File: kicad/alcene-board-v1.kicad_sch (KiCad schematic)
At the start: 3 parts, among them J1 ESP32-S3-DevKitC-1_J1, J3 ESP32-S3-DevKitC-1_J3, J4 ILI9341_TFT_14pin

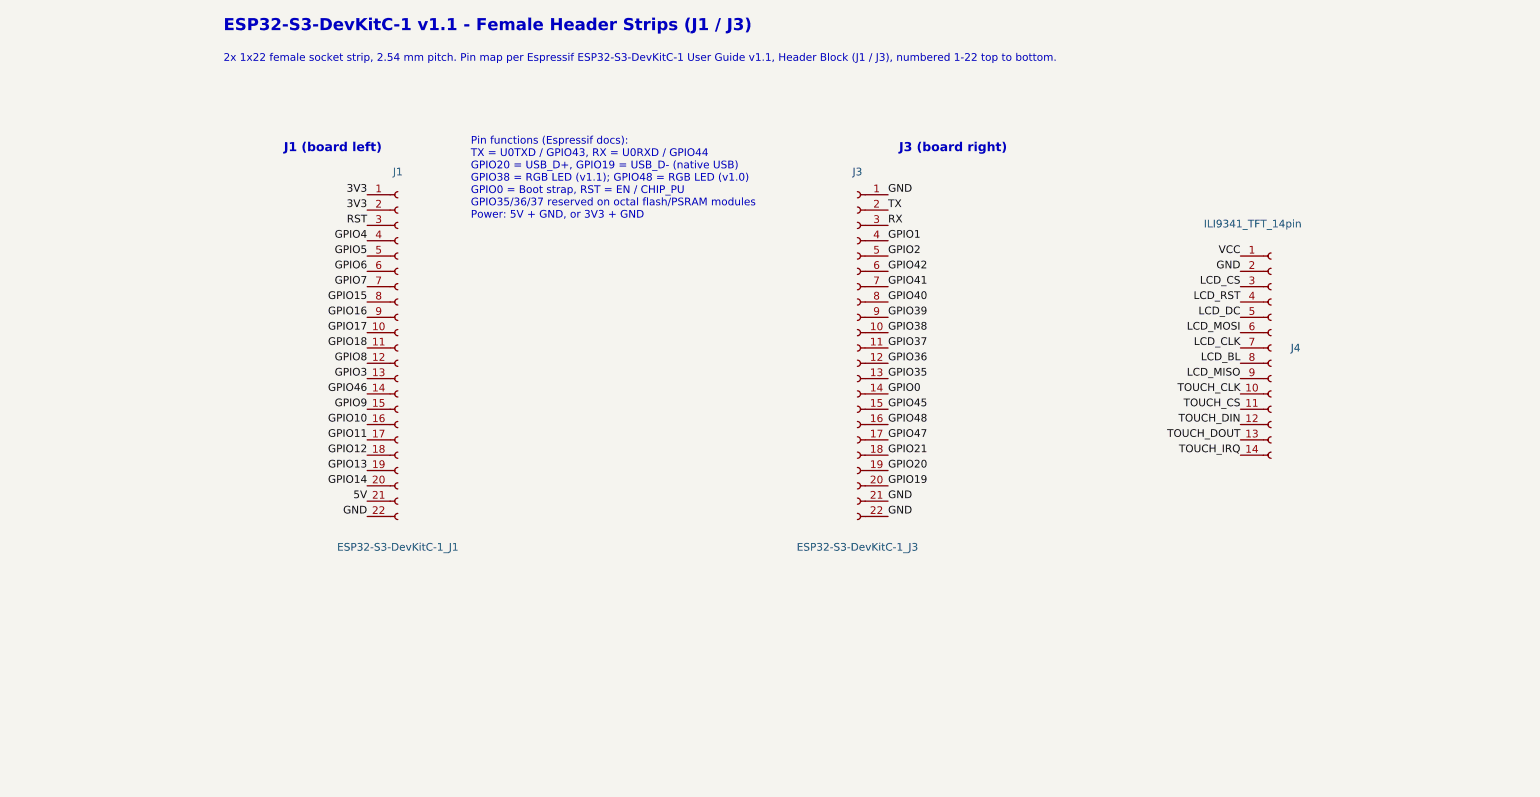
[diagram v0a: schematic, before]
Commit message: feat: wiring ILI9341 pin labels to ESP32 S3
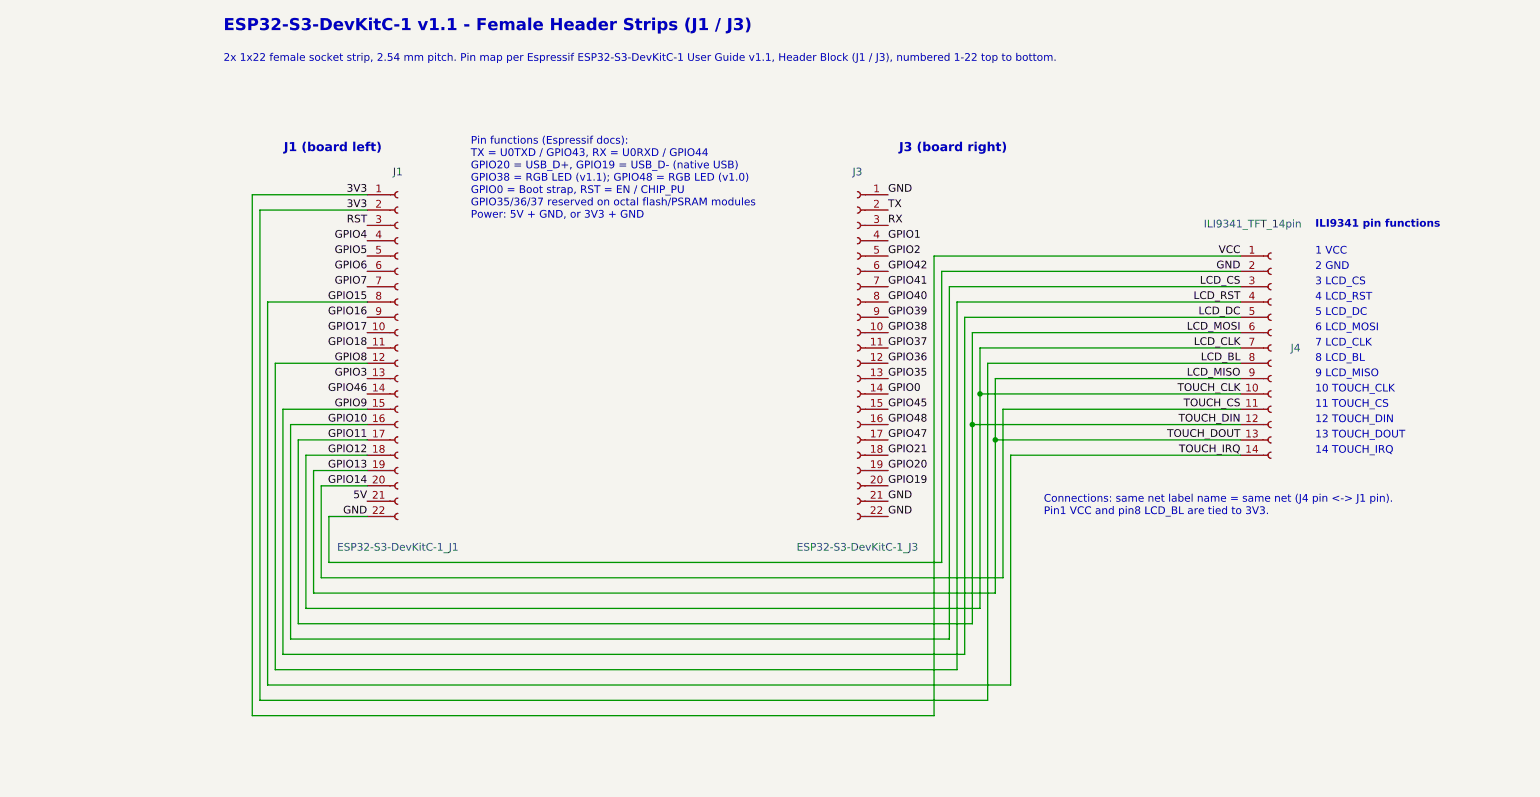
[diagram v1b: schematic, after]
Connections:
- net LCD_BL is gone; now on net 3V3: J4.8 (Pin_8)
- net LCD_CLK is gone; now on net GPIO12: J4.7 (Pin_7)
- net LCD_CS is gone; now on net GPIO10: J4.3 (Pin_3)
- net LCD_DC is gone; now on net GPIO9: J4.5 (Pin_5)
- net LCD_MISO is gone; now on net GPIO13: J4.9 (Pin_9)
- net LCD_MOSI is gone; now on net GPIO11: J4.6 (Pin_6)
- net LCD_RST is gone; now on net GPIO8: J4.4 (Pin_4)
- net TOUCH_CLK is gone; now on net GPIO12: J4.10 (Pin_10)
- net TOUCH_CS is gone; now on net GPIO14: J4.11 (Pin_11)
- net TOUCH_DIN is gone; now on net GPIO11: J4.12 (Pin_12)
- net TOUCH_DOUT is gone; now on net GPIO13: J4.13 (Pin_13)
- net TOUCH_IRQ is gone; now on net GPIO15: J4.14 (Pin_14)
- net VCC is gone; now on net 3V3: J4.1 (Pin_1)
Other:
- note added: "1 VCC"
- note added: "10 TOUCH_CLK"
- note added: "11 TOUCH_CS"
- note added: "12 TOUCH_DIN"
- note added: "13 TOUCH_DOUT"
- note added: "14 TOUCH_IRQ"
- note added: "2 GND"
- note added: "3 LCD_CS"
- note added: "4 LCD_RST"
- note added: "5 LCD_DC"
- note added: "6 LCD_MOSI"
- note added: "7 LCD_CLK"
- note added: "8 LCD_BL"
- note added: "9 LCD_MISO"
- note added: "Connections: same net label name = same net (J4 pin <-> J1 pin). Pin1 VCC and pin8 LCD_BL are tied to 3V3."
- note added: "ILI9341 pin functions"

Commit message: feat: wiring TFT and ESP32 headers and labels
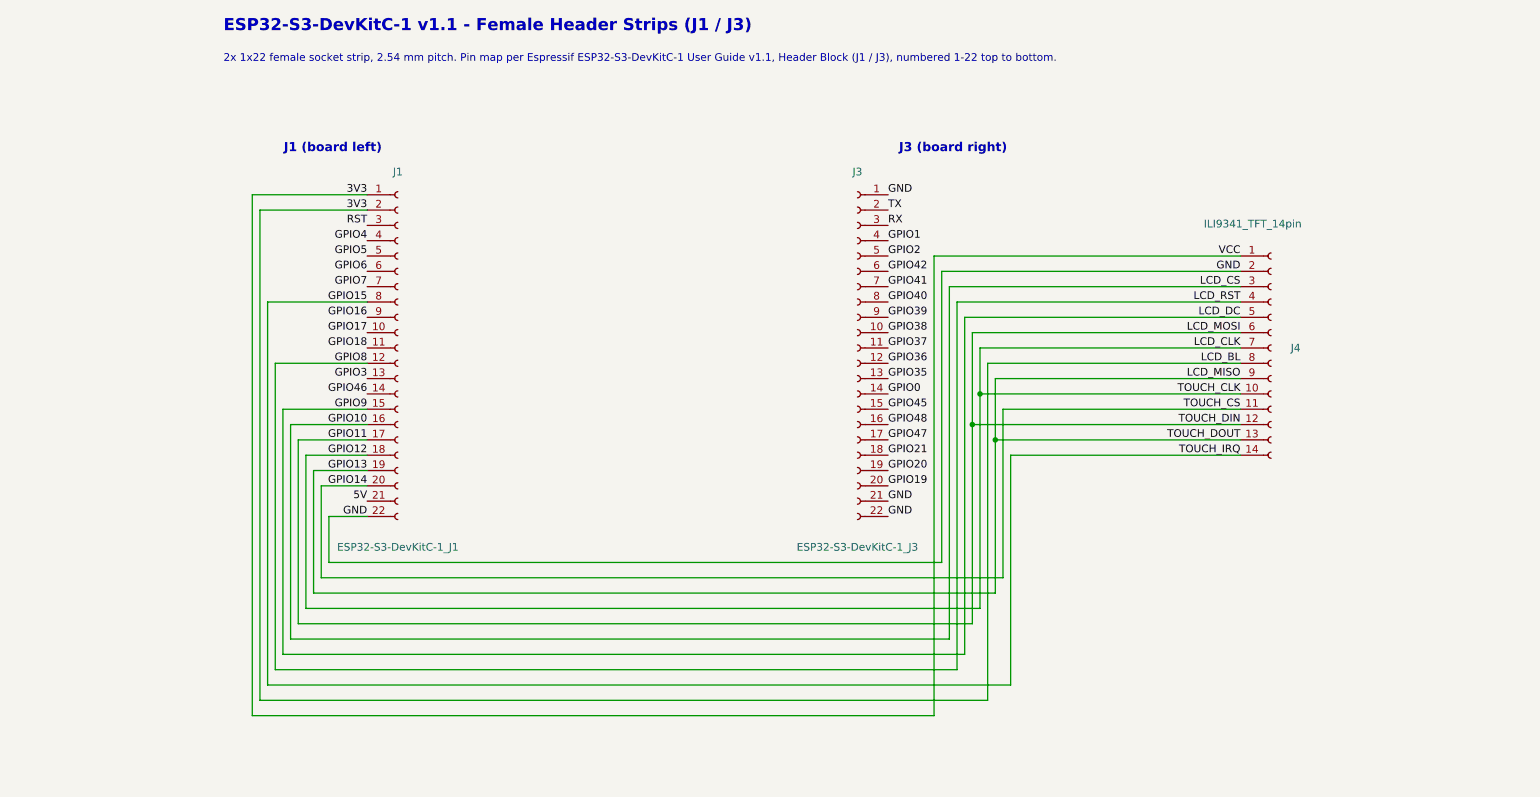
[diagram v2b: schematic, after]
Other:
- note removed: "1 VCC"
- note removed: "10 TOUCH_CLK"
- note removed: "11 TOUCH_CS"
- note removed: "12 TOUCH_DIN"
- note removed: "13 TOUCH_DOUT"
- note removed: "14 TOUCH_IRQ"
- note removed: "2 GND"
- note removed: "3 LCD_CS"
- note removed: "4 LCD_RST"
- note removed: "5 LCD_DC"
- note removed: "6 LCD_MOSI"
- note removed: "7 LCD_CLK"
- note removed: "8 LCD_BL"
- note removed: "9 LCD_MISO"
- note removed: "Connections: same net label name = same net (J4 pin <-> J1 pin). Pin1 VCC and pin8 LCD_BL are tied to 3V3."
- note removed: "ILI9341 pin functions"
- note removed: "Pin functions (Espressif docs): TX = U0TXD / GPIO43, RX = U0RXD / GPIO44 GPIO20 = USB_D+, GPIO19 = USB_D- (native USB) GPIO38 = RGB LED (v1.1); GPIO48 = RGB LED (v1.0) GPIO0 = Boot strap, RST = EN / CHIP_PU GPIO35/36/37 reserved on octal flash/PSRAM modules Power: 5V + GND, or 3V3 + GND"

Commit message: feat: Add USB-C connector, capacitor, and resistor symbols to schematic librar
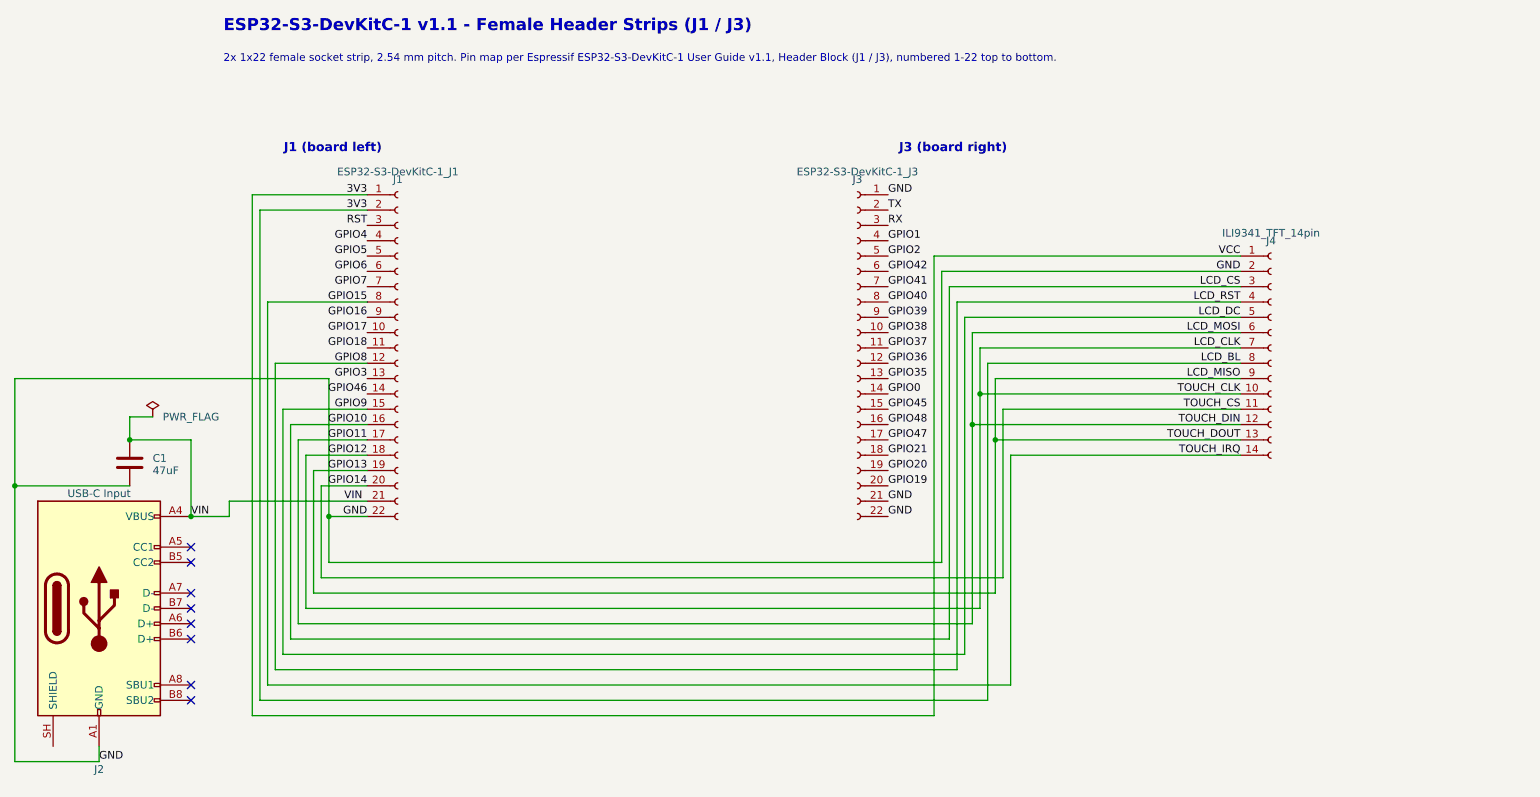
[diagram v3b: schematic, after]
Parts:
- added C1: 47uF, Capacitor_SMD:C_0805_2012Metric, symbol Device:C
- added J2: USB-C Input, Connector_USB:USB_C_Receptacle_GCT_USB4085, symbol Connector:USB_C_Receptacle_USB2.0_16P
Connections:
- net GND: now also C1.2, J2.A1 (GND), J2.A12 (GND), J2.B1 (GND), J2.B12 (GND)
- net 5V renamed VIN
- net VIN: now also C1.1, J2.A4 (VBUS), J2.A9 (VBUS), J2.B4 (VBUS), J2.B9 (VBUS)
- no-connect marks 0 -> 8

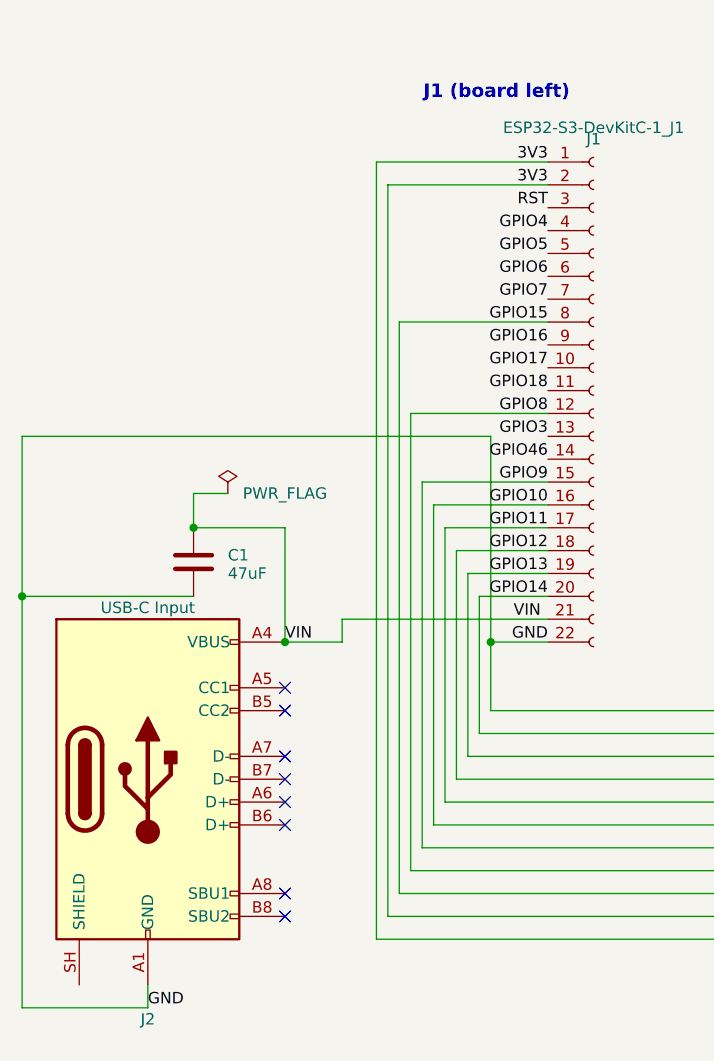
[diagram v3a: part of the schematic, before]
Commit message: feat: USB Type C input
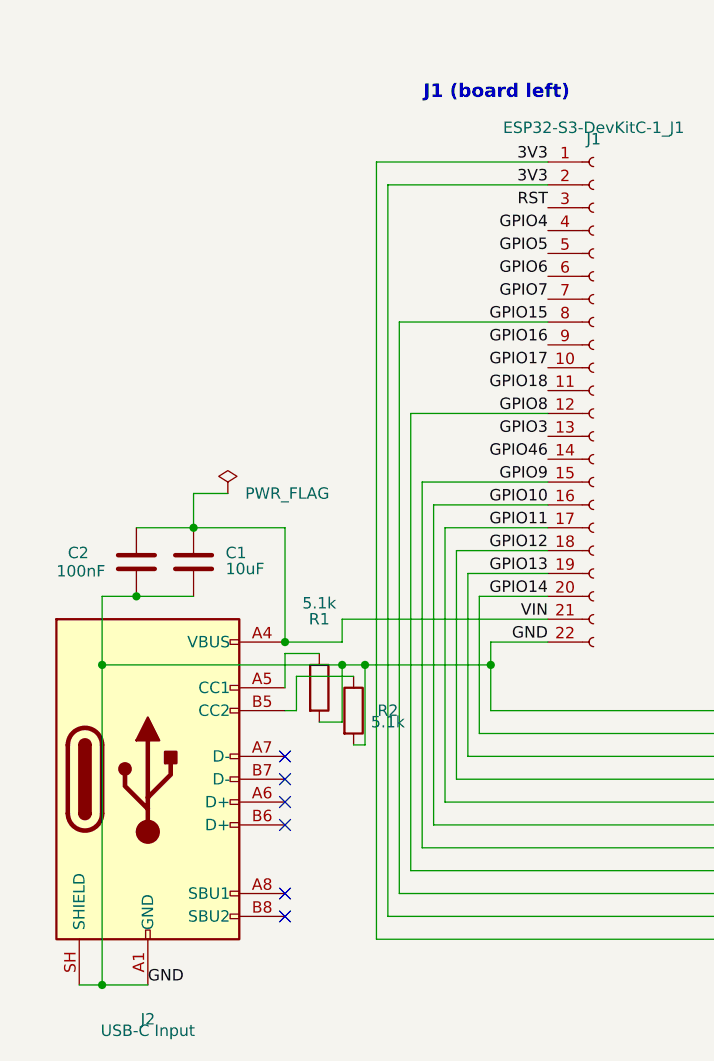
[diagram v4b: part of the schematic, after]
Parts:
- added C2: 100nF, Capacitor_SMD:C_0805_2012Metric, symbol Device:C
- added R1, R2: 5.1k, Resistor_SMD:R_0805_2012Metric, symbol Device:R
- C1: value 47uF -> 10uF
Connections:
- net GND: now also J2.SH (SHIELD), C2.2, R1.2, R2.2
- net VIN: now also C2.1
- net at J2.A5 (CC1): now also R1.1
- net at J2.B5 (CC2): now also R2.1
- no-connect marks 8 -> 6

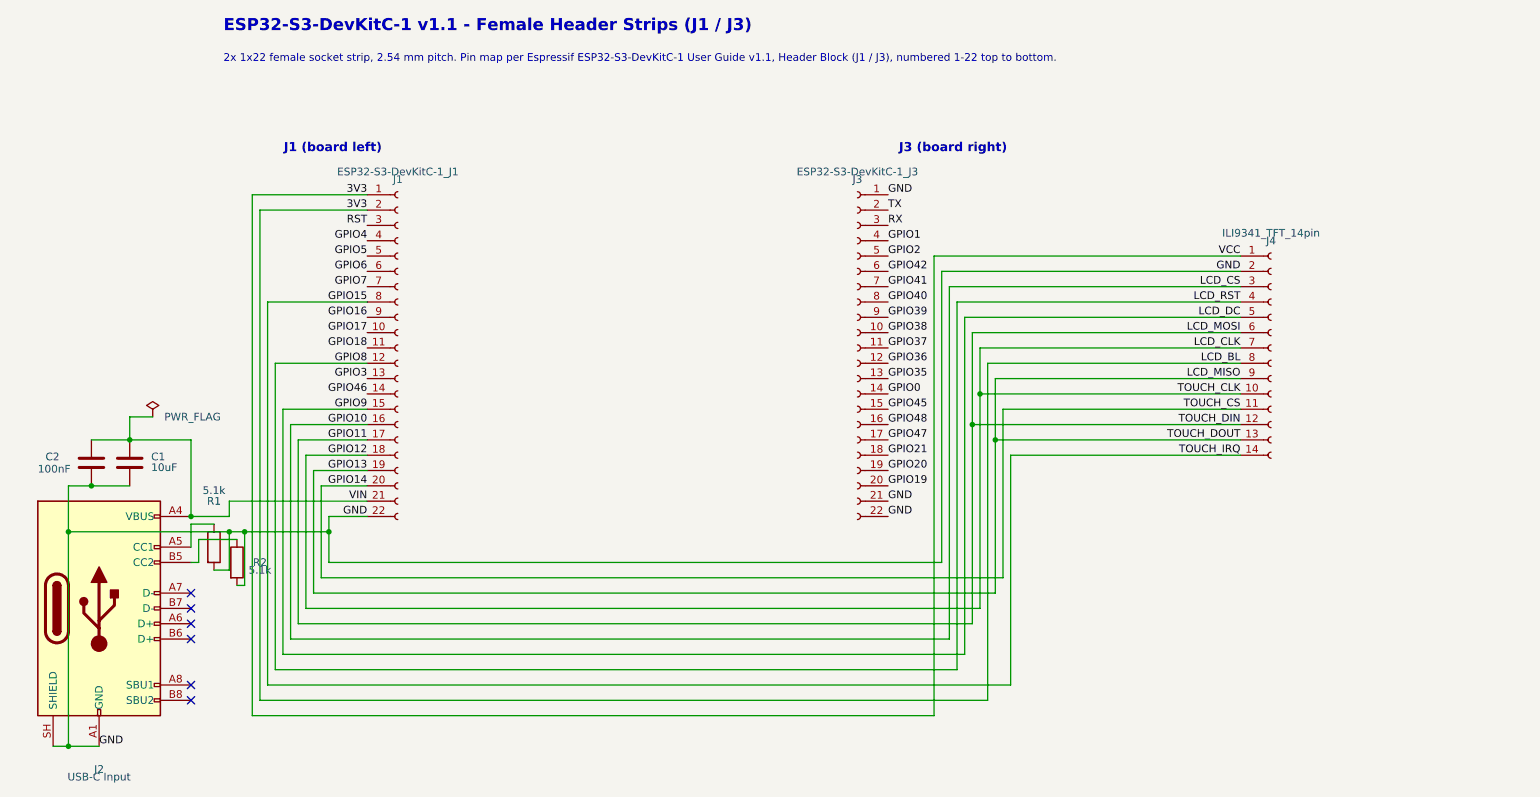
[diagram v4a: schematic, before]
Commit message: feat: Update schematic to A3 paper size and simplify wires
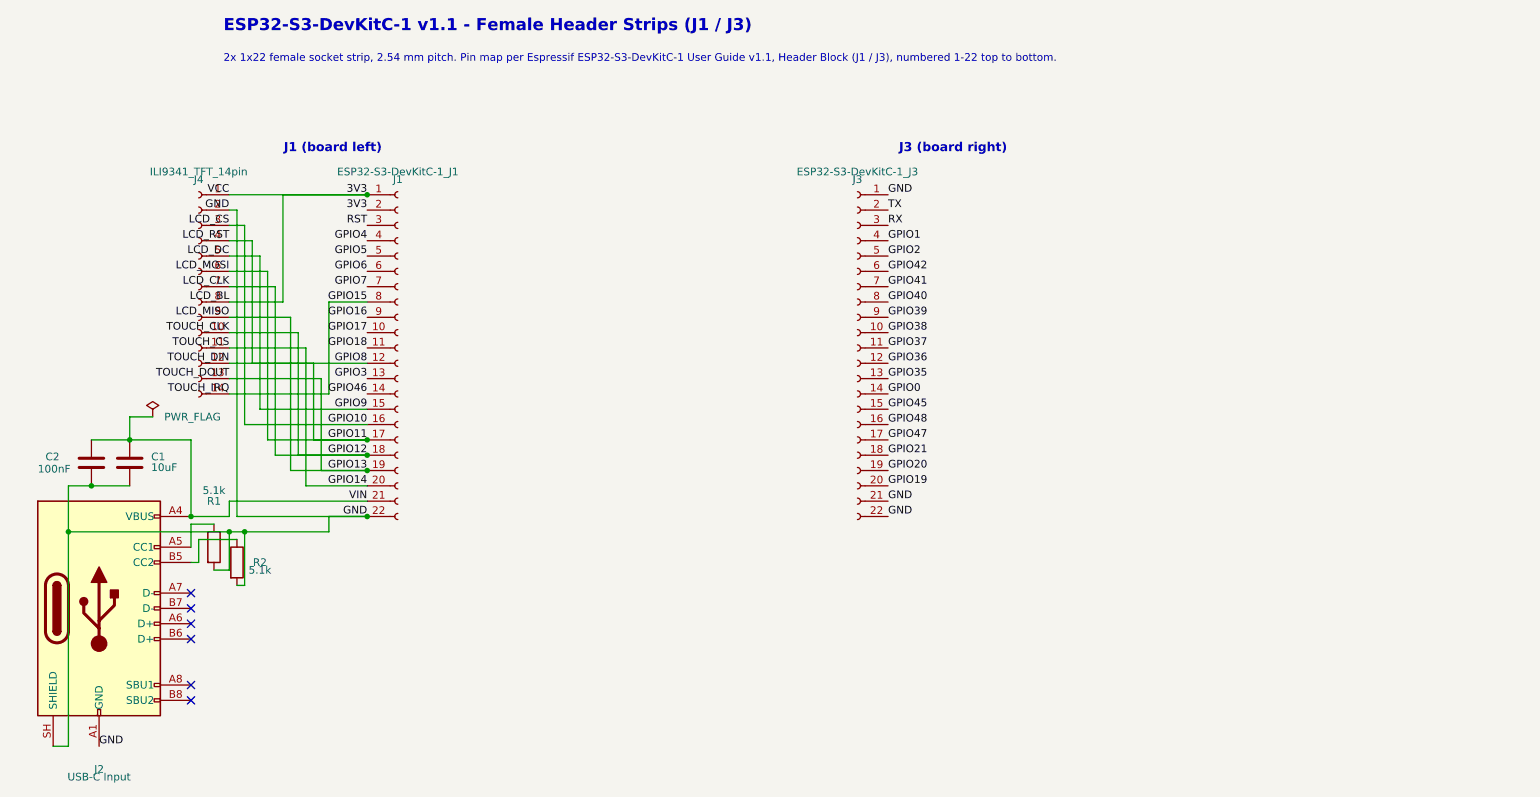
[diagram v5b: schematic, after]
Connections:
- net GPIO8 is gone; now on net GPIO11: J1.12 (Pin_12), J4.4 (Pin_4)
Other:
- moved on the sheet: J4
